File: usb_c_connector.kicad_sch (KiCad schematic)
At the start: 24 parts, among them J4 USB_C_Receptacle_USB2.0_16P, J5 USB_C_Receptacle_USB2.0_16P, U6 LM66100DCK, U7 LM66100DCK, U8 USBLC6-2SC6, U9 USBLC6-2SC6

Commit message: Assign footprints and parts
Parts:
- C26, C27, C28, C29, C30, C32, C34, C35: footprint Capacitor_SMD:C_0402_1005Metric_Pad0.74x0.62mm_HandSolder -> Capacitor_SMD:C_0603_1608Metric_Pad1.08x0.95mm_HandSolder; LCSC Part (none) -> C14663
- C31, C33: LCSC Part (none) -> C96446
- R13, R14, R15, R16: footprint (none) -> Resistor_SMD:R_0603_1608Metric_Pad0.98x0.95mm_HandSolder; LCSC Part (none) -> C105580
- R17, R18: footprint (none) -> Resistor_SMD:R_0603_1608Metric_Pad0.98x0.95mm_HandSolder; LCSC Part (none) -> C105578
- TP10, TP9: footprint (none) -> TestPoint:TestPoint_Pad_D1.5mm
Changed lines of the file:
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@@
 			)
 		)
-		(property "Footprint" ""
+		(property "Footprint" "Resistor_SMD:R_0603_1608Metric_Pad0.98x0.95mm_HandSolder"
 			(at 86.36 102.108 90)
 			(effects
@@
 			)
 		)
+		(property "LCSC Part" "C105580"
+			(at 86.36 100.33 90)
+			(effects
+				(font
+					(size 1.27 1.27)
+				)
+				(hide yes)
+			)
+		)
 		(pin "2"
 		)
@@
 			)
 		)
-		(property "Footprint" ""
+		(property "Footprint" "Resistor_SMD:R_0603_1608Metric_Pad0.98x0.95mm_HandSolder"
 			(at 198.12 102.108 90)
 			(effects
@@
 			)
 		)
+		(property "LCSC Part" "C105580"
+			(at 198.12 100.33 90)
+			(effects
+				(font
+					(size 1.27 1.27)
+				)
+				(hide yes)
+			)
+		)
 		(pin "2"
 		)
@@
 			)
 		)
+		(property "LCSC Part" "C96446"
+			(at 247.65 96.52 0)
+			(effects
+				(font
+					(size 1.27 1.27)
+				)
+				(hide yes)
+			)
+		)
 		(pin "1"
 		)
@@
 			)
 		)
-		(property "Footprint" "Capacitor_SMD:C_0402_1005Metric_Pad0.74x0.62mm_HandSolder"
+		(property "Footprint" "Capacitor_SMD:C_0603_1608Metric_Pad1.08x0.95mm_HandSolder"
 			(at 114.6048 58.42 0)
 			(effects
@@
 			)
 		)
+		(property "LCSC Part" "C14663"
+			(at 115.57 54.61 0)
+			(effects
+				(font
+					(size 1.27 1.27)
+				)
+				(hide yes)
+			)
+		)
 		(pin "1"
 		)
@@
 			)
 		)
-		(property "Footprint" "Capacitor_SMD:C_0402_1005Metric_Pad0.74x0.62mm_HandSolder"
+		(property "Footprint" "Capacitor_SMD:C_0603_1608Metric_Pad1.08x0.95mm_HandSolder"
 			(at 165.4048 143.51 0)
 			(effects
@@
 			)
 		)
+		(property "LCSC Part" "C14663"
+			(at 166.37 139.7 0)
+			(effects
+				(font
+					(size 1.27 1.27)
+				)
+				(hide yes)
+			)
+		)
 		(pin "2"
 		)
@@
 			)
 		)
-		(property "Footprint" ""
+		(property "Footprint" "TestPoint:TestPoint_Pad_D1.5mm"
 			(at 67.31 54.61 0)
 			(effects
@@
 			)
 		)
-		(property "Footprint" "Capacitor_SMD:C_0402_1005Metric_Pad0.74x0.62mm_HandSolder"
+		(property "Footprint" "Capacitor_SMD:C_0603_1608Metric_Pad1.08x0.95mm_HandSolder"
 			(at 227.6348 58.42 0)
 			(effects
@@
 			)
 		)
+		(property "LCSC Part" "C14663"
+			(at 228.6 54.61 0)
+			(effects
+				(font
+					(size 1.27 1.27)
+				)
+				(hide yes)
+			)
+		)
 		(pin "1"
 		)
@@
 			)
 		)
-		(property "Footprint" "Capacitor_SMD:C_0402_1005Metric_Pad0.74x0.62mm_HandSolder"
+		(property "Footprint" "Capacitor_SMD:C_0603_1608Metric_Pad1.08x0.95mm_HandSolder"
 			(at 234.6452 100.33 0)
 			(effects
@@
 			)
 		)
+		(property "LCSC Part" "C14663"
+			(at 233.68 96.52 0)
+			(effects
+				(font
+					(size 1.27 1.27)
+				)
+				(hide yes)
+			)
+		)
 		(pin "2"
 		)
@@
 			)
 		)
-		(property "Footprint" "Capacitor_SMD:C_0402_1005Metric_Pad0.74x0.62mm_HandSolder"
+		(property "Footprint" "Capacitor_SMD:C_0603_1608Metric_Pad1.08x0.95mm_HandSolder"
 			(at 175.5648 58.42 0)
 			(effects
@@
 			)
 		)
+		(property "LCSC Part" "C14663"
+			(at 176.53 54.61 0)
+			(effects
+				(font
+					(size 1.27 1.27)
+				)
+				(hide yes)
+			)
+		)
 		(pin "1"
 		)
@@
 			)
 		)
-		(property "Footprint" ""
+		(property "Footprint" "TestPoint:TestPoint_Pad_D1.5mm"
 			(at 180.34 54.61 0)
 			(effects
@@
 			)
 		)
-		(property "Footprint" ""
+		(property "Footprint" "Resistor_SMD:R_0603_1608Metric_Pad0.98x0.95mm_HandSolder"
 			(at 198.12 104.648 90)
 			(effects
@@
 			)
 		)
+		(property "LCSC Part" "C105580"
+			(at 198.12 102.87 90)
+			(effects
+				(font
+					(size 1.27 1.27)
+				)
+				(hide yes)
+			)
+		)
 		(pin "2"
 		)
@@
 			)
 		)
-		(property "Footprint" "Capacitor_SMD:C_0402_1005Metric_Pad0.74x0.62mm_HandSolder"
+		(property "Footprint" "Capacitor_SMD:C_0603_1608Metric_Pad1.08x0.95mm_HandSolder"
 			(at 53.6448 143.51 0)
 			(effects
@@
 			)
 		)
+		(property "LCSC Part" "C14663"
+			(at 54.61 139.7 0)
+			(effects
+				(font
+					(size 1.27 1.27)
+				)
+				(hide yes)
+			)
+		)
 		(pin "2"
 		)
@@
 			)
 		)
-		(property "Footprint" ""
+		(property "Footprint" "Resistor_SMD:R_0603_1608Metric_Pad0.98x0.95mm_HandSolder"
 			(at 86.36 104.648 90)
 			(effects
@@
 			)
 		)
+		(property "LCSC Part" "C105580"
+			(at 86.36 102.87 90)
+			(effects
+				(font
+					(size 1.27 1.27)
+				)
+				(hide yes)
+			)
+		)
 		(pin "2"
 		)
@@
 			)
 		)
-		(property "Footprint" "Capacitor_SMD:C_0402_1005Metric_Pad0.74x0.62mm_HandSolder"
+		(property "Footprint" "Capacitor_SMD:C_0603_1608Metric_Pad1.08x0.95mm_HandSolder"
 			(at 63.8048 58.42 0)
 			(effects
@@
 			)
 		)
+		(property "LCSC Part" "C14663"
+			(at 64.77 54.61 0)
+			(effects
+				(font
+					(size 1.27 1.27)
+				)
+				(hide yes)
+			)
+		)
 		(pin "1"
 		)
@@
 			)
 		)
-		(property "Footprint" ""
+		(property "Footprint" "Resistor_SMD:R_0603_1608Metric_Pad0.98x0.95mm_HandSolder"
 			(at 173.228 139.7 90)
 			(effects
@@
 			)
 		)
+		(property "LCSC Part" "C105578"
+			(at 171.45 139.7 0)
+			(effects
+				(font
+					(size 1.27 1.27)
+				)
+				(hide yes)
+			)
+		)
 		(pin "1"
 		)
@@
 			)
 		)
-		(property "Footprint" ""
+		(property "Footprint" "Resistor_SMD:R_0603_1608Metric_Pad0.98x0.95mm_HandSolder"
 			(at 61.468 139.7 90)
 			(effects
@@
 			)
 		)
+		(property "LCSC Part" "C105578"
+			(at 59.69 139.7 0)
+			(effects
+				(font
+					(size 1.27 1.27)
+				)
+				(hide yes)
+			)
+		)
 		(pin "1"
 		)
@@
 			)
 		)
+		(property "LCSC Part" "C96446"
+			(at 135.89 96.52 0)
+			(effects
+				(font
+					(size 1.27 1.27)
+				)
+				(hide yes)
+			)
+		)
 		(pin "1"
 		)
@@
 			)
 		)
-		(property "Footprint" "Capacitor_SMD:C_0402_1005Metric_Pad0.74x0.62mm_HandSolder"
+		(property "Footprint" "Capacitor_SMD:C_0603_1608Metric_Pad1.08x0.95mm_HandSolder"
 			(at 122.8852 100.33 0)
 			(effects
@@
 			(at 121.92 96.52 0)
 			(effects
+				(font
+					(size 1.27 1.27)
+				)
+				(hide yes)
+			)
+		)
+		(property "LCSC Part" "C14663"
+			(at 121.92 96.52 0)
+			(effects

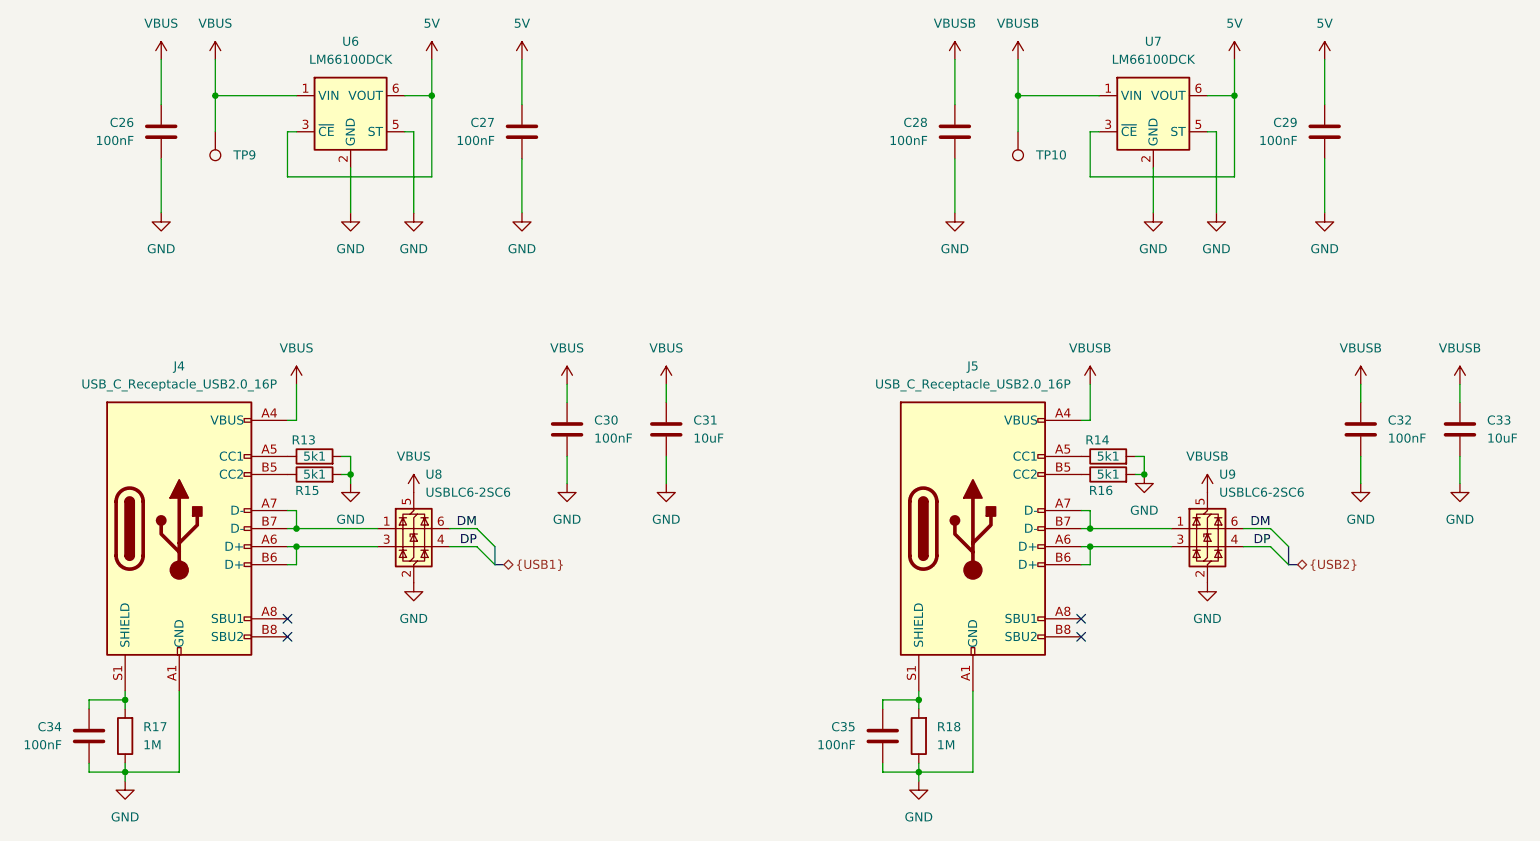
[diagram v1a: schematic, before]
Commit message: De-cascade buck converters
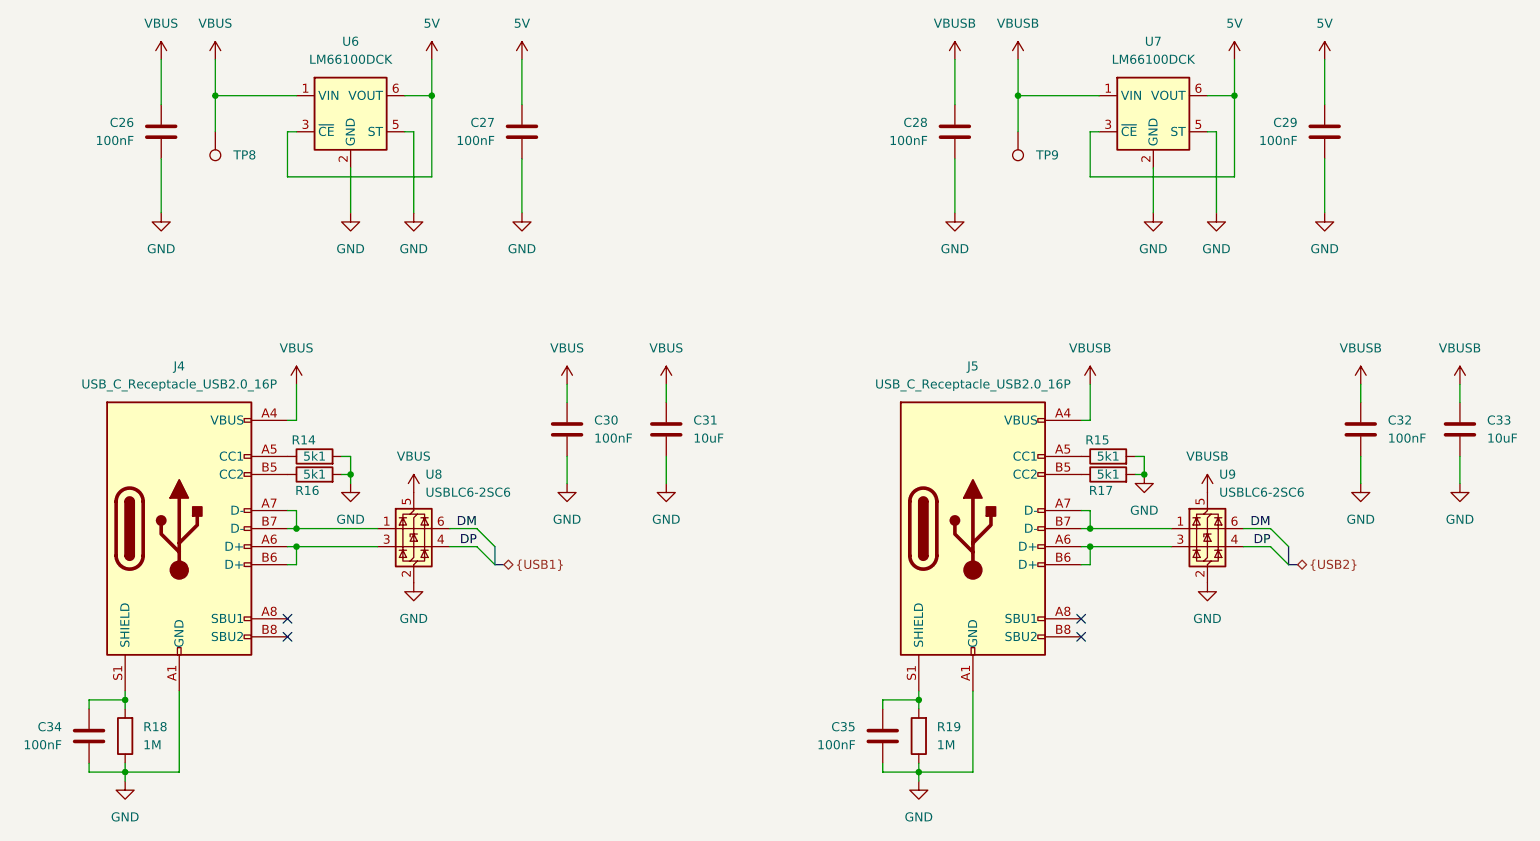
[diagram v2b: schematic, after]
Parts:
- renumbered R13 to R14, R14 to R15, R15 to R16, R16 to R17, R17 to R18, R18 to R19, TP9 to TP8, TP10 to TP9

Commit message: Break out motor encoder signals
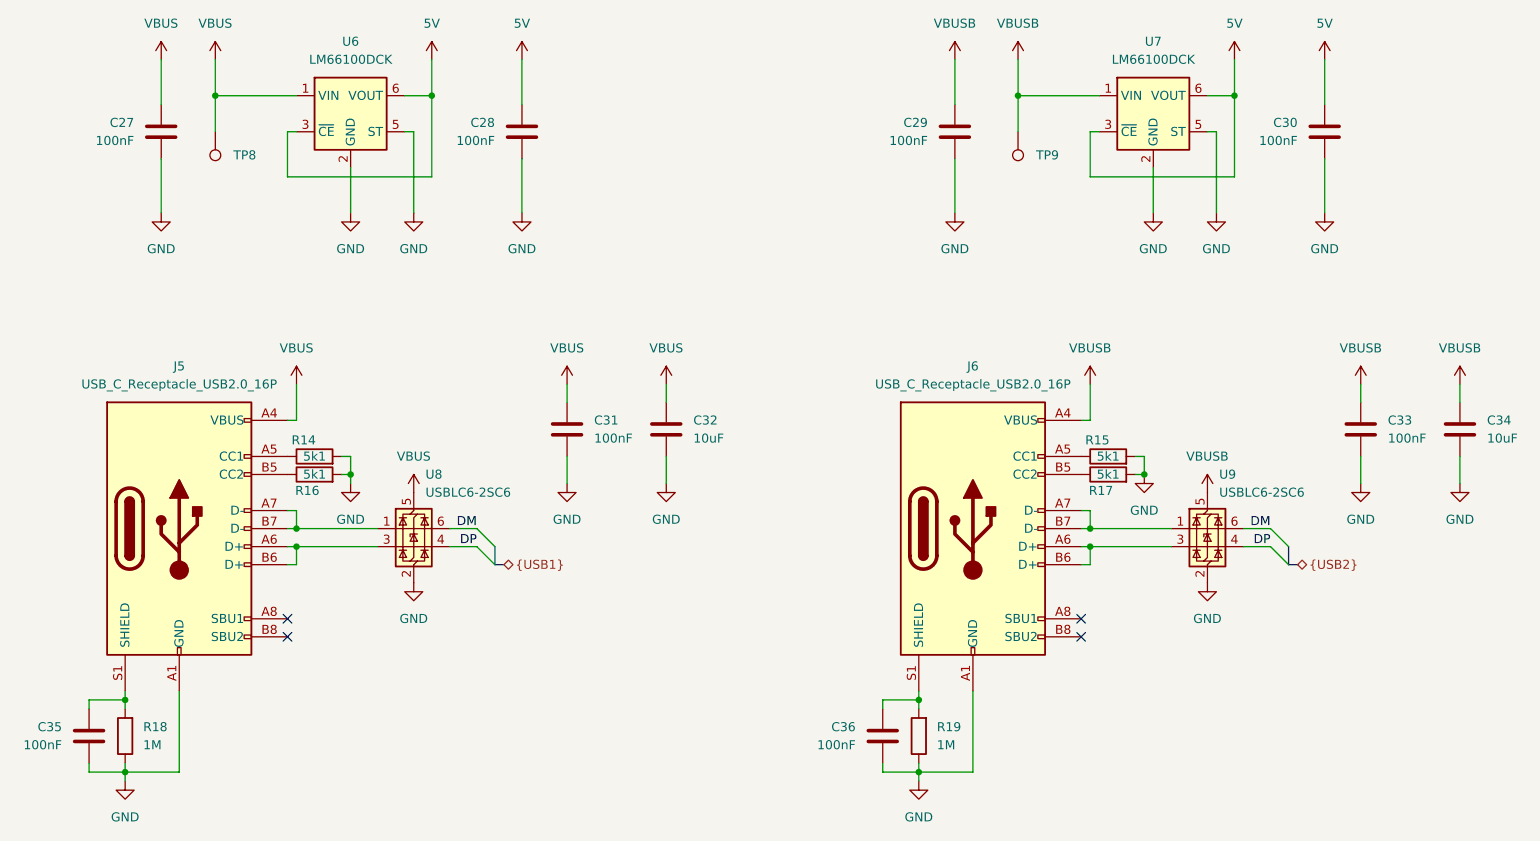
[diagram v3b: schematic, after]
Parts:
- renumbered C26 to C27, C27 to C28, C28 to C29, C29 to C30, C30 to C31, C31 to C32, C32 to C33, C33 to C34, C34 to C35, C35 to C36, J4 to J5, J5 to J6

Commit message: Make lcsc field compatible with plugin
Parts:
- C27, C28, C29, C30, C31, C33, C35, C36: LCSC PN (none) -> C14663; LCSC Part C14663 -> (none)
- C32, C34: LCSC PN (none) -> C96446; LCSC Part C96446 -> (none)
- J5, J6: LCSC PN (none) -> C709357; LCSC Part C709357 -> (none)
- R14, R15, R16, R17: LCSC PN (none) -> C105580; LCSC Part C105580 -> (none)
- R18, R19: LCSC PN (none) -> C105578; LCSC Part C105578 -> (none)
- U6, U7: LCSC PN (none) -> C2869734; LCSC Part C2869734 -> (none)
- U8, U9: LCSC PN (none) -> C7519; LCSC Part C7519 -> (none)
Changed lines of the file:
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@@
 			)
 		)
-		(property "LCSC Part" "C7519"
+		(property "LCSC PN" "C7519"
 			(at 100.33 110.49 0)
 			(effects
@@
 			)
 		)
-		(property "LCSC Part" "C105580"
+		(property "LCSC PN" "C105580"
 			(at 86.36 100.33 90)
 			(effects
@@
 			)
 		)
-		(property "LCSC Part" "C105580"
+		(property "LCSC PN" "C105580"
 			(at 198.12 100.33 90)
 			(effects
@@
 			)
 		)
-		(property "LCSC Part" "C96446"
+		(property "LCSC PN" "C96446"
 			(at 247.65 96.52 0)
 			(effects
@@
 			)
 		)
-		(property "LCSC Part" "C14663"
+		(property "LCSC PN" "C14663"
 			(at 115.57 54.61 0)
 			(effects
@@
 			)
 		)
-		(property "LCSC Part" "C14663"
+		(property "LCSC PN" "C14663"
 			(at 166.37 139.7 0)
 			(effects
@@
 			)
 		)
-		(property "LCSC Part" "C709357"
+		(property "LCSC PN" "C709357"
 			(at 179.07 110.49 0)
 			(effects
@@
 			)
 		)
-		(property "LCSC Part" "C14663"
+		(property "LCSC PN" "C14663"
 			(at 228.6 54.61 0)
 			(effects
@@
 			)
 		)
-		(property "LCSC Part" "C14663"
+		(property "LCSC PN" "C14663"
 			(at 233.68 96.52 0)
 			(effects
@@
 			)
 		)
-		(property "LCSC Part" "C2869734"
+		(property "LCSC PN" "C2869734"
 			(at 91.44 52.07 0)
 			(effects
@@
 			)
 		)
-		(property "LCSC Part" "C709357"
+		(property "LCSC PN" "C709357"
 			(at 67.31 110.49 0)
 			(effects
@@
 			)
 		)
-		(property "LCSC Part" "C14663"
+		(property "LCSC PN" "C14663"
 			(at 176.53 54.61 0)
 			(effects
@@
 			)
 		)
-		(property "LCSC Part" "C105580"
+		(property "LCSC PN" "C105580"
 			(at 198.12 102.87 90)
 			(effects
@@
 			)
 		)
-		(property "LCSC Part" "C14663"
+		(property "LCSC PN" "C14663"
 			(at 54.61 139.7 0)
 			(effects
@@
 			)
 		)
-		(property "LCSC Part" "C105580"
+		(property "LCSC PN" "C105580"
 			(at 86.36 102.87 90)
 			(effects
@@
 			)
 		)
-		(property "LCSC Part" "C14663"
+		(property "LCSC PN" "C14663"
 			(at 64.77 54.61 0)
 			(effects
@@
 			)
 		)
-		(property "LCSC Part" "C105578"
+		(property "LCSC PN" "C105578"
 			(at 171.45 139.7 0)
 			(effects
@@
 			)
 		)
-		(property "LCSC Part" "C105578"
+		(property "LCSC PN" "C105578"
 			(at 59.69 139.7 0)
 			(effects
@@
 			)
 		)
-		(property "LCSC Part" "C96446"
+		(property "LCSC PN" "C96446"
 			(at 135.89 96.52 0)
 			(effects
@@
 			)
 		)
-		(property "LCSC Part" "C14663"
+		(property "LCSC PN" "C14663"
 			(at 121.92 96.52 0)
 			(effects
@@
 			)
 		)
-		(property "LCSC Part" "C7519"
+		(property "LCSC PN" "C7519"
 			(at 212.09 110.49 0)
 			(effects
@@
 			)
 		)
-		(property "LCSC Part" "C2869734"
+		(property "LCSC PN" "C2869734"
 			(at 204.47 52.07 0)
 			(effects

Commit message: Exclude test points from BOM
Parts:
- TP8, TP9: now left out of the parts list
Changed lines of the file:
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@@
 		(unit 1)
 		(exclude_from_sim no)
-		(in_bom yes)
+		(in_bom no)
 		(on_board yes)
 		(dnp no)
@@
 		(unit 1)
 		(exclude_from_sim no)
-		(in_bom yes)
-		(on_board yes)
-		(dnp no)
+		(in_bom no)
+		(on_board yes)
+		(dnp no)
